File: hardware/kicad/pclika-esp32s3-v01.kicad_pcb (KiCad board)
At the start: 4 copper layers, 65 x 45 mm, 42 parts, among them J1 USB-C Receptacle, J2 I2C JST SH 4P, Q1 MMBT3904, Q2 MMBT3904, SW1 SW_BOOT, SW2 SW_RST, SW3 SW_USER, U1 ESP32-S3-WROOM-1, U2 AMS1117-3.3, U3 USBLC6-2SC6, U4 CH340C

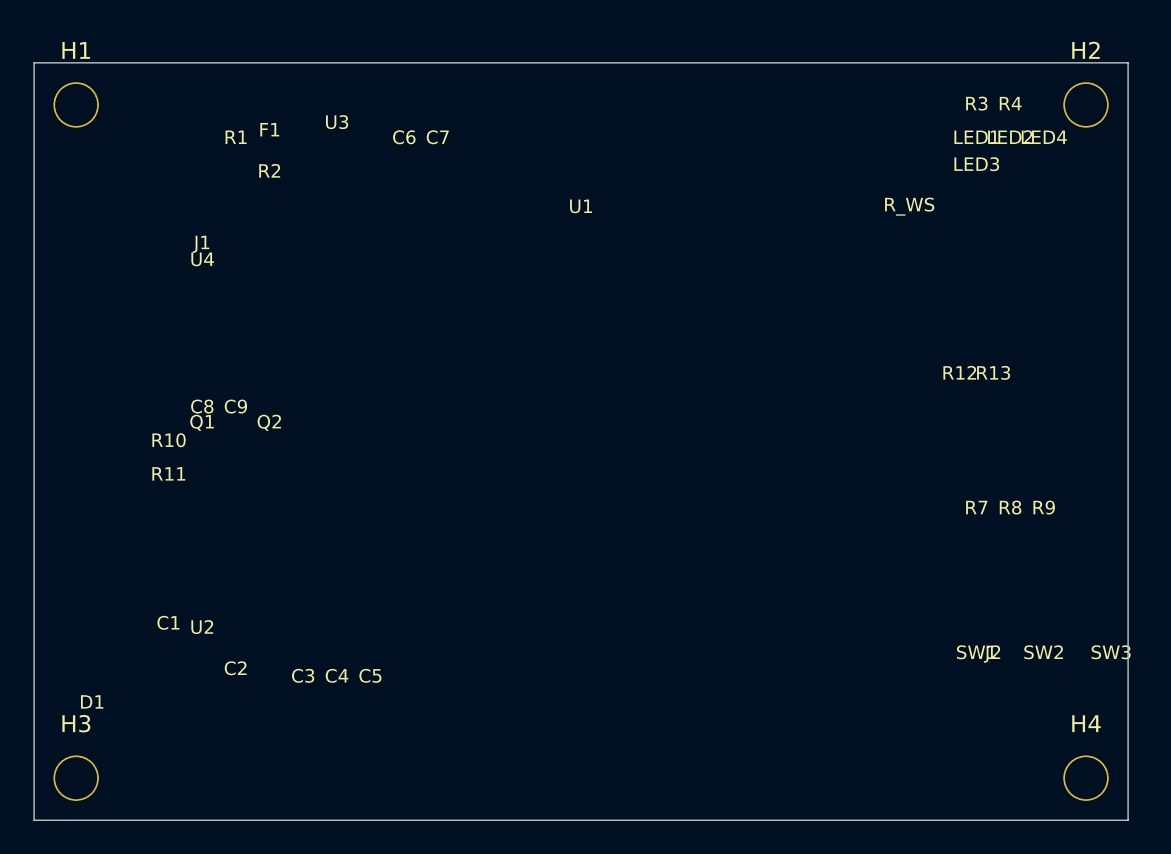
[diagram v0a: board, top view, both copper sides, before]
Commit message: fix(hardware): remove placeholder footprints from PCB file
Removed 38 Pclika:*_placeholder footprints that caused KiCad to report
'library not found' errors on file open. PCB now contains only:
- Board outline (Edge.Cuts, 65x45mm)
- GND and +3V3 copper pours
- 4x M2.5 mounting holes (MountingHole:MountingHole_2.7mm_M2.5)
- Net classes and DRC rules

Workflow: open pclika-esp32s3-v01.kicad_pro in KiCad 8, then
Tools > Update PCB from Schematic (Ctrl+U) to import all footprints
from schematic with correct pads and net assignments.
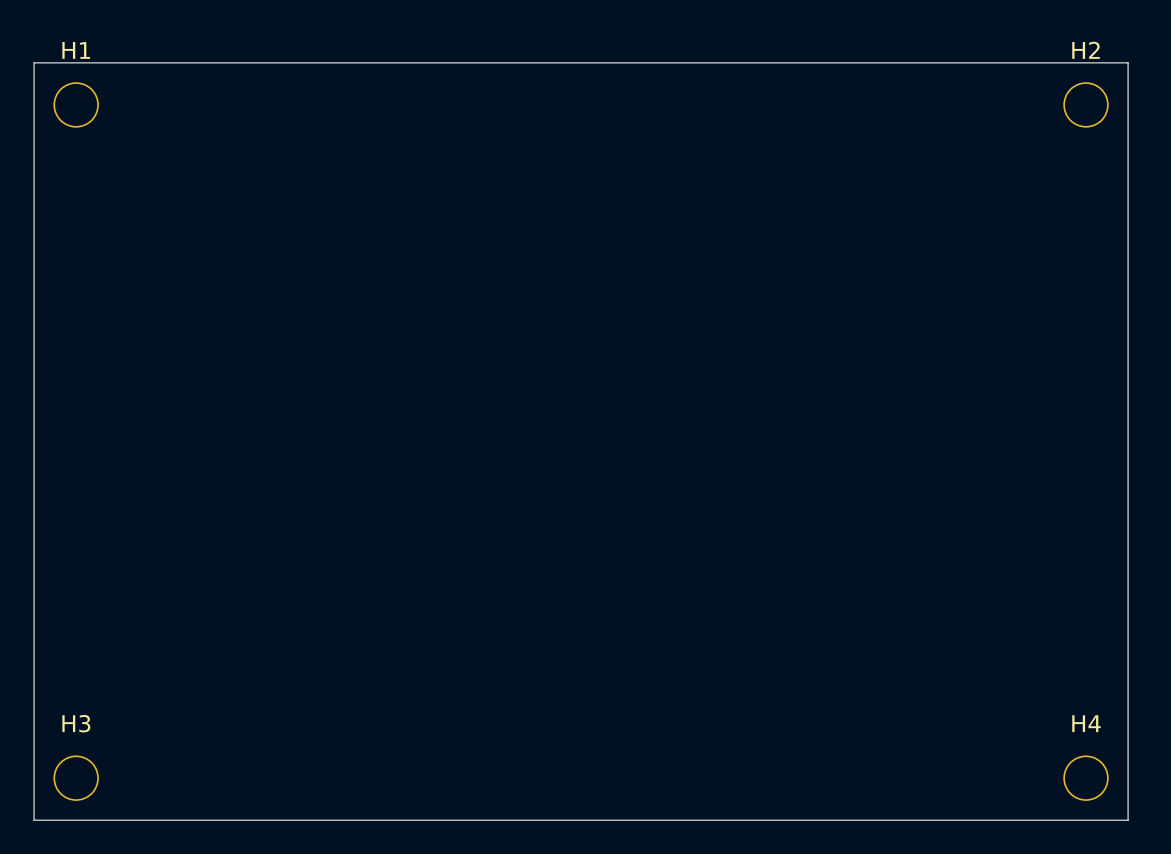
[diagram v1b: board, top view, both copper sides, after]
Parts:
- removed C1: 100uF Elec, Pclika:C1_placeholder
- removed C2: 10uF 0805, Pclika:C2_placeholder
- removed C3: 100nF 0402, Pclika:C3_placeholder
- removed C4: 100nF 0402, Pclika:C4_placeholder
- removed C5: 100nF 0402, Pclika:C5_placeholder
- removed C6: 100nF USB D+, Pclika:C6_placeholder
- removed C7: 100nF USB D-, Pclika:C7_placeholder
- removed C8: 100nF CH340 VBUS, Pclika:C8_placeholder
- removed C9: 100nF CH340 3V3, Pclika:C9_placeholder
- removed D1: SS14, Pclika:D1_placeholder
- removed F1: Polyfuse 500mA, Pclika:F1_placeholder
- removed J1: USB-C Receptacle, Pclika:J1_placeholder
- removed J2: I2C JST SH 4P, Pclika:J2_placeholder
- removed LED1: LED Green 0402, Pclika:LED1_placeholder
- removed LED2: LED Blue 0402, Pclika:LED2_placeholder
- removed LED3: WS2812B-2020, Pclika:LED3_placeholder
- removed LED4: LED Red 0402, Pclika:LED4_placeholder
- removed Q1: MMBT3904, Pclika:Q1_placeholder
- removed Q2: MMBT3904, Pclika:Q2_placeholder
- removed R1: 5.1k CC1, Pclika:R1_placeholder
- removed R10: 330 DTR, Pclika:R10_placeholder
- removed R11: 330 RTS, Pclika:R11_placeholder
- removed R12: 4.7k I2C SDA, Pclika:R12_placeholder
- removed R13: 4.7k I2C SCL, Pclika:R13_placeholder
- removed R2: 5.1k CC2, Pclika:R2_placeholder
- removed R3: 1k LED PWR, Pclika:R3_placeholder
- removed R4: 330 LED RUN, Pclika:R4_placeholder
- removed R7: 10k RST PU, Pclika:R7_placeholder
- removed R8: 10k BOOT PU, Pclika:R8_placeholder
- removed R9: 10k EN PU, Pclika:R9_placeholder
- removed R_WS: 470 WS2812, Pclika:R_WS_placeholder
- removed SW1: SW_BOOT, Pclika:SW1_placeholder
- removed SW2: SW_RST, Pclika:SW2_placeholder
- removed SW3: SW_USER, Pclika:SW3_placeholder
- removed U1: ESP32-S3-WROOM-1, Pclika:U1_placeholder
- removed U2: AMS1117-3.3, Pclika:U2_placeholder
- removed U3: USBLC6-2SC6, Pclika:U3_placeholder
- removed U4: CH340C, Pclika:U4_placeholder
